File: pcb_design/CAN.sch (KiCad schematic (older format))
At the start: 9 parts, among them Q2 2N7002PW, U2 ISO1050

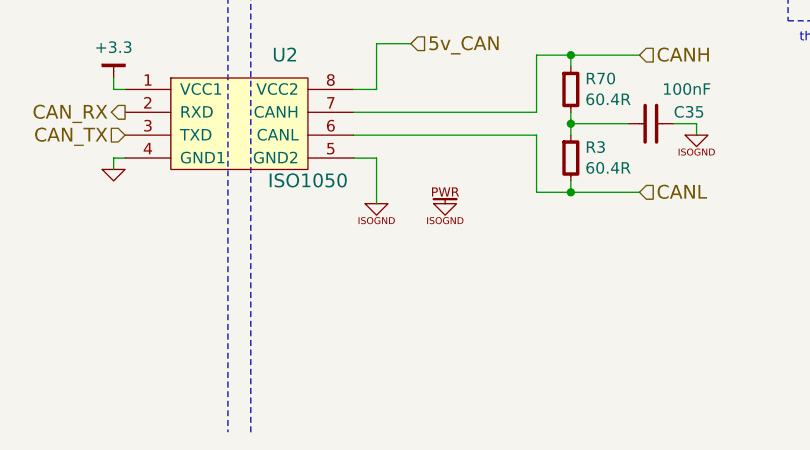
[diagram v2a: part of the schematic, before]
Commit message: Updated layout. DRC OK, moved silkscreen, bumped version to 0.2. Added portable 3d models
Signed-off-by: Marcos Chaparro <mchaparro@paltatech.com>
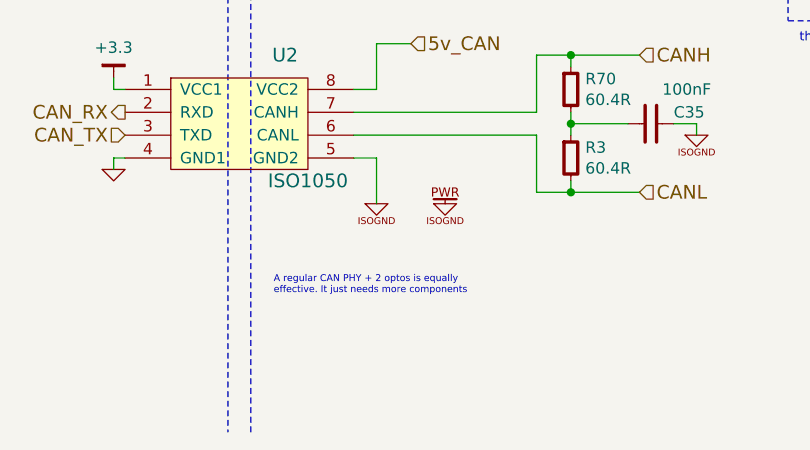
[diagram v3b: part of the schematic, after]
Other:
- note added: "A regular CAN PHY + 2 optos is equally\neffective. It just needs more components"
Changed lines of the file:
@@
 Connection ~ 8200 3300
 Connection ~ 8500 3300
+Text Notes 5650 4800 0    30   ~ 0
+A regular CAN PHY + 2 optos is equally\neffective. It just needs more components
 $EndSCHEMATC

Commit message: Added RC filter to FAULT line to prevent noise triggering it
Signed-off-by: Marcos Chaparro <mchaparro@paltatech.com>
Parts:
- C1, C35: BOM CAP MLCC 100pF C0G 50V 5% [0603] -> CAP MLCC 100nF C0G 50V 5% [0603]
- C401: BOM (none) -> CAP MLCC 100nF C0G 50V 5% [0603]
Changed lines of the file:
@@
 F 7 "490-1524-1-ND" H 0   0   50  0001 C CNN "SPN"
 F 8 "" H 0   0   50  0001 C CNN "SPURL"
+F 9 "CAP MLCC 100nF C0G 50V 5% [0603]" H 0   0   60  0001 C CNN "BOM"
 	1    4000 4050
 	1    0    0    -1
@@
 F 2 "IPC7351-Nominal:CAPC1608X55" H 7250 3150 50  0001 C CNN
 F 3 "http://www.murata.com/~/media/webrenewal/support/library/catalog/products/capacitor/mlcc/c02e.ashx" H 7240 3125 60  0001 C CNN
-F 4 "CAP MLCC 100pF C0G 50V 5% [0603]" H 8050 3700 60  0001 C CNN "BOM"
+F 4 "CAP MLCC 100nF C0G 50V 5% [0603]" H 8050 3700 60  0001 C CNN "BOM"
 F 5 "Murata Electronics North America" H 0   0   50  0001 C CNN "MFR"
 F 6 "GRM188R71E104KA01D" H 0   0   50  0001 C CNN "MPN"
@@
 F 2 "IPC7351-Nominal:CAPC1608X55" H 7300 4050 50  0001 C CNN
 F 3 "http://www.murata.com/~/media/webrenewal/support/library/catalog/products/capacitor/mlcc/c02e.ashx" H 7290 4025 60  0001 C CNN
-F 4 "CAP MLCC 100pF C0G 50V 5% [0603]" H 8100 4600 60  0001 C CNN "BOM"
+F 4 "CAP MLCC 100nF C0G 50V 5% [0603]" H 8100 4600 60  0001 C CNN "BOM"
 F 5 "Murata Electronics North America" H 0   0   50  0001 C CNN "MFR"
 F 6 "GRM188R71E104KA01D" H 0   0   50  0001 C CNN "MPN"
